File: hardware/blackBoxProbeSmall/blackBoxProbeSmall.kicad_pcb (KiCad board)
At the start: 4 copper layers, 44 x 29 mm, 79 parts, among them J1 USB-ID, J2 JTAG_2X05, J3 JTAG_2X05, J4 DevBoardUartInput, Q1 Q_NMOS_DUAL, Q2 Q_PMOS_DUAL, U1 MCP1702-MB, U2 USBLC6-2, U3 STM32F103CBT, U4 74X2T45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

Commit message: WIP routing/placement
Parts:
- removed R1, R13, R14, R15, R17, R19, R2, R21, R24, R25, R3, R4, R8, R9: 33, SquantorRcl:R_0402_hand
- removed R29, R30, R31, R32: 330, SquantorRcl:R_0402_hand
- removed R37, R38: 10K, SquantorRcl:R_0402_hand
- added RN1: 470, Resistor_SMD:R_Array_Convex_4x0402, F.Cu at (146.8, 106.8)
- added RN2: 47K, Resistor_SMD:R_Array_Convex_4x0402, F.Cu at (129.8, 98.8)
- added RN3: 33, Resistor_SMD:R_Array_Convex_4x0402, F.Cu at (129.8, 101.8)
- added RN4: 33, Resistor_SMD:R_Array_Convex_4x0402, F.Cu at (161.9, 96.7)
- J1: footprint SquantorUsb:SquantorUsb-USB-UB-SMD4H -> SquantorUsb:USB-muB-SMD_TH
- J4: value DevBoardUartInput -> DevBoardUartOutput
- N2: value V20190815 -> V20200131; footprint SquantorLabels:Label_version -> SquantorLabels:Label_Generic; moved to B.Cu
- moved R6 25.0 mm to (147.3, 87.6), turned to 270 degrees
- moved S1 24.5 mm to (152.2, 88.2)
- moved DA1 23.7 mm to (147.2, 110.7), turned to 0 degrees
- moved Q1 17.2 mm to (158.9, 88.9)
- moved R20 13.1 mm to (162.0, 94.7), turned to 0 degrees
- moved C14 12.5 mm to (153.1, 90.9), turned to 0 degrees
- moved F2 11.5 mm to (164.6, 101.7)
- moved R5 9.90 mm to (161.6, 105.4)
- moved Q2 5.38 mm to (156.0, 107.7)
- moved R28 5.38 mm to (153.7, 107.5)
- moved R10 0.74 mm to (161.6, 109.3), turned to 180 degrees
- moved C11 0.74 mm to (161.0, 111.0)
- moved R11 0.74 mm to (162.1, 111.0)
- moved N2 0.71 mm to (141.1, 95.7), turned to 180 degrees
- moved R33 0.20 mm to (161.6, 107.4)
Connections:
- J2 pad 2: /MCU_TMS -> Net-(J2-Pad2)
- J2 pad 4: /MCU_TCK -> Net-(J2-Pad4)
- J2 pad 6: /MCU_TDO -> Net-(J2-Pad6)
- J2 pad 7: Net-(J2-Pad7) -> (no net)
- J2 pad 8: /MCU_TDI -> Net-(J2-Pad8)
- J3 pad 4: /PROBE_E_TCK -> Net-(J3-Pad4)
- J3 pad 7: Net-(J3-Pad7) -> (no net)
- J3 pad 8: /PROBE_E_TDI -> Net-(J3-Pad8)
- J4 pad 4: /PROBE_E_TX -> Net-(J4-Pad4)
- R5 pad 1: /PROBE_E_TX -> Net-(J4-Pad4)
- R5 pad 2: Net-(R5-Pad2) -> /PROBE_E_TX
- U3 pad 10: Net-(U3-Pad10) -> (no net)
- U3 pad 11: Net-(R14-Pad1) -> /PROBE_TMS_DIR
- U3 pad 13: Net-(R15-Pad1) -> /PROBE_I_TDI
- U3 pad 14: Net-(R17-Pad1) -> /PROBE_I_TMS
- U3 pad 15: Net-(R19-Pad1) -> /PROBE_I_TCK
- U3 pad 2: Net-(U3-Pad2) -> (no net)
- U3 pad 27: Net-(U3-Pad27) -> (no net)
- U3 pad 28: Net-(U3-Pad28) -> (no net)
- U3 pad 3: Net-(U3-Pad3) -> (no net)
- U3 pad 30: Net-(R21-Pad1) -> /PROBE_I_TX
- U3 pad 39: Net-(R1-Pad1) -> /MCU_TDO
- U3 pad 4: Net-(U3-Pad4) -> (no net)
- U3 pad 43: Net-(U3-Pad43) -> (no net)
- U3 pad 45: Net-(U3-Pad45) -> (no net)
- U3 pad 46: Net-(U3-Pad46) -> (no net)
- U4 pad 6: Net-(R5-Pad2) -> /PROBE_E_TX
- U5 pad 6: Net-(R9-Pad2) -> /PROBE_E_TDI
- U5 pad 7: Net-(R8-Pad2) -> /PROBE_E_TCK
- U6 pad 2: Net-(R3-Pad1) -> /PROBE_I_TDO
- U6 pad 3: Net-(R4-Pad1) -> /PROBE_I_RX
- U7 pad 3: Net-(R2-Pad1) -> /PROBE_I_TMS
- U7 pad 6: Net-(R13-Pad2) -> /PROBE_E_TMS
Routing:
- net /PROBE_VDD: track 0.00 -> 24.2 mm
- net /BUTTON: track 17.3 -> 0.00 mm
- net /USB_PU: track 0.00 -> 14.4 mm
- net /USB_V: track 1.10 -> 14.0 mm
- net /MCU_RST: track 0.00 -> 12.1 mm, vias 0 -> 2
- net Net-(J2-Pad8): track 0.00 -> 4.92 mm
- net /MCU_TDI: track 8.99 -> 4.51 mm, vias 0 -> 1
- net Net-(J2-Pad6): track 0.00 -> 4.38 mm
- net Net-(J2-Pad4): track 0.00 -> 4.22 mm
- net Net-(J2-Pad2): track 0.00 -> 4.22 mm
- net Net-(R1-Pad1): track 3.76 -> 0.00 mm
- net /VSS: track 51.4 -> 48.3 mm, vias 14 -> 15
- net Net-(R21-Pad1): track 2.72 -> 0.00 mm
- net /PROBE_I_TDO: track 2.45 -> 0.00 mm
- net Net-(R15-Pad1): track 2.42 -> 0.00 mm
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
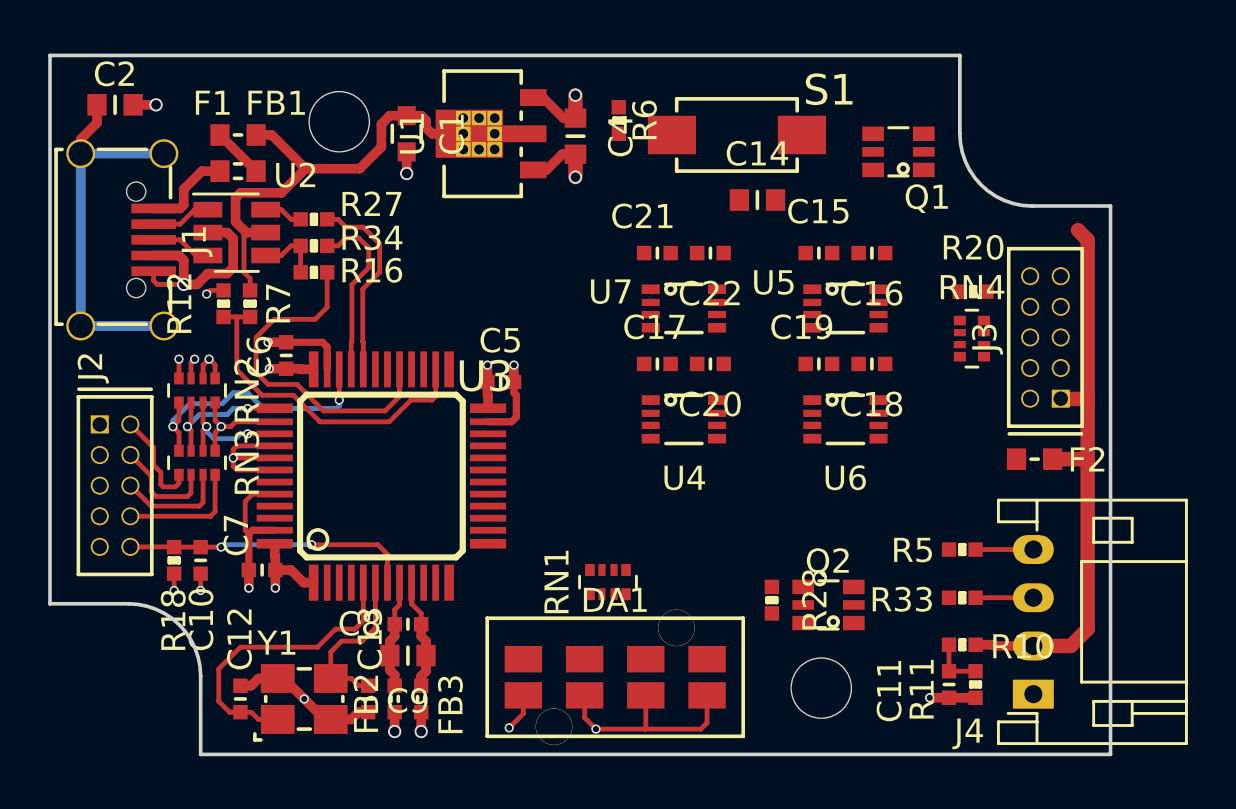
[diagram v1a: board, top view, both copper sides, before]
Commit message: WIP place/route, starting with level shifters
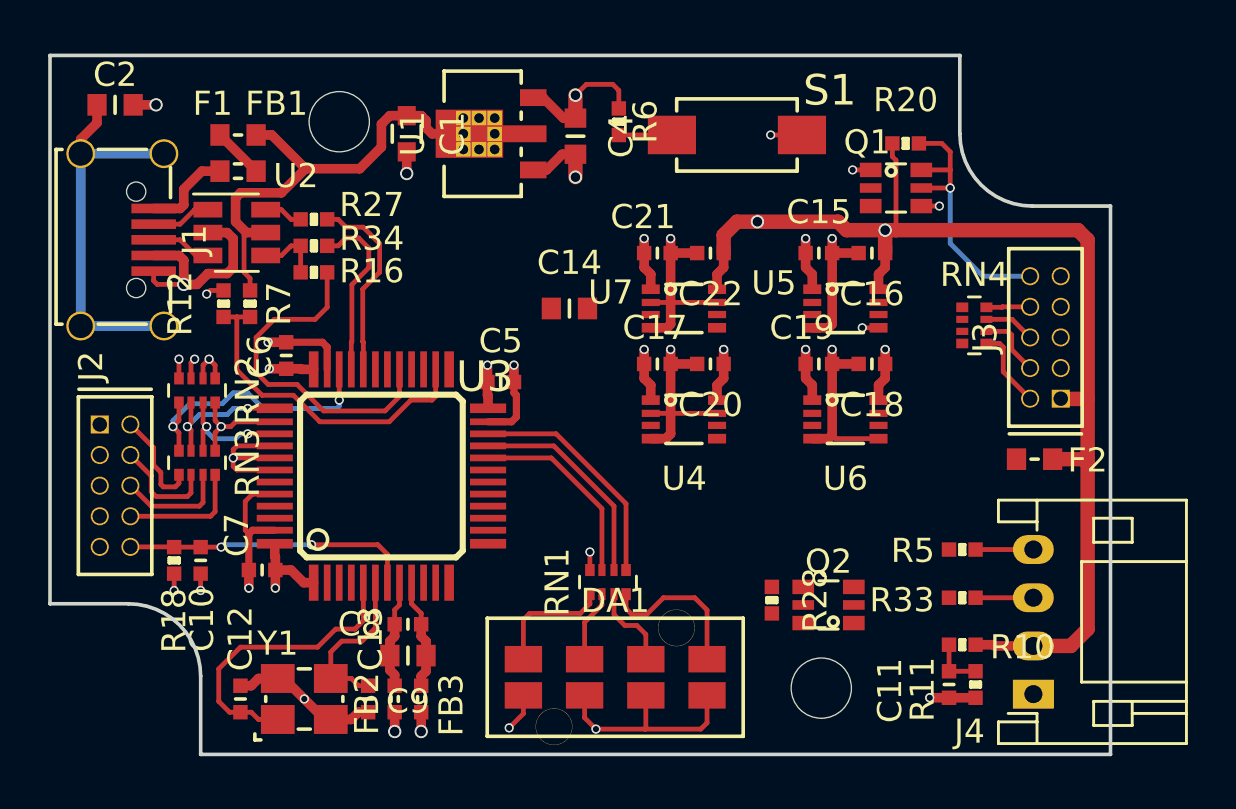
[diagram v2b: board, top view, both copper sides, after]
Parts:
- moved C14 9.00 mm to (145.2, 95.4)
- moved R20 6.76 mm to (159.2, 88.5)
- moved Q1 1.50 mm to (158.8, 90.4), turned to 270 degrees
- moved RN4 0.56 mm to (162.1, 96.1)
- moved R6 0.05 mm to (147.3, 87.7)
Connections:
- RN1 pad 1: Net-(DA1-Pad4) -> Net-(DA1-Pad1)
- RN1 pad 2: Net-(DA1-Pad3) -> Net-(DA1-Pad2)
- RN1 pad 3: Net-(DA1-Pad2) -> Net-(DA1-Pad3)
- RN1 pad 4: Net-(DA1-Pad1) -> Net-(DA1-Pad4)
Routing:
- net /PROBE_VDD: track 24.2 -> 64.0 mm, vias 0 -> 4
- net /VSS: track 48.3 -> 80.8 mm, vias 15 -> 22
- net /VDD: track 20.5 -> 33.5 mm, vias 9 -> 15
- net /PROBE_E_RST: track 0.00 -> 11.5 mm, vias 0 -> 1
- net /LED2: track 0.00 -> 9.68 mm
- net /LED1: track 0.00 -> 8.91 mm
- net /LED0: track 0.00 -> 8.14 mm
- net Net-(DA1-Pad4): track 0.00 -> 6.60 mm
- net Net-(DA1-Pad1): track 0.00 -> 5.07 mm
- net Net-(DA1-Pad3): track 0.00 -> 3.54 mm
- net Net-(J3-Pad2): track 0.00 -> 3.36 mm
- net Net-(DA1-Pad2): track 0.00 -> 3.00 mm
- net Net-(J3-Pad4): track 0.00 -> 2.80 mm
- net /BUTTON: track 0.00 -> 2.20 mm
- net Net-(J3-Pad6): track 0.00 -> 2.13 mm
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
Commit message: done place and route, silk placement starting
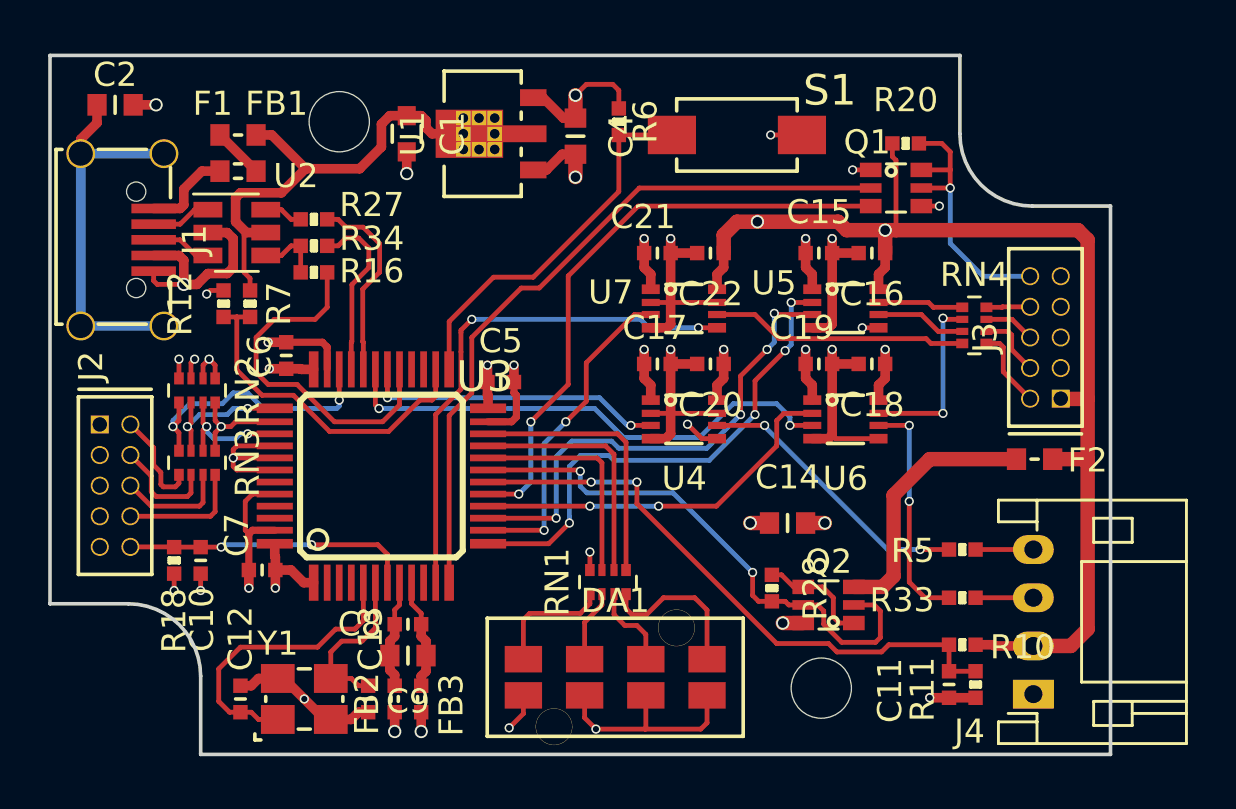
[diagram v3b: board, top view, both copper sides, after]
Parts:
- moved C14 12.7 mm to (154.3, 104.3)
- moved R28 0.50 mm to (153.7, 107.0)
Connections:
- U5 pad 2: /PROBE_I_TCK -> /PROBE_I_TDI
- U5 pad 3: /PROBE_I_TDI -> /PROBE_I_TCK
- U5 pad 6: /PROBE_E_TDI -> /PROBE_E_TCK
- U5 pad 7: /PROBE_E_TCK -> /PROBE_E_TDI
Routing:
- net /PROBE_I_RST: track 0.00 -> 29.7 mm
- net /PROBE_I_RST_SEN: track 0.00 -> 24.9 mm, vias 0 -> 2
- net /TARGET_PWR_EN: track 0.00 -> 22.9 mm, vias 0 -> 2
- net /TARGET_PWR_SENSE: track 2.20 -> 24.9 mm, vias 0 -> 2
- net /PROBE_TMS_DIR: track 0.00 -> 21.9 mm, vias 0 -> 2
- net /PROBE_I_RX: track 0.00 -> 21.3 mm, vias 0 -> 2
- net /PROBE_I_TDI: track 0.00 -> 21.0 mm, vias 0 -> 4
- net /PROBE_I_TCK: track 0.00 -> 20.4 mm, vias 0 -> 4
- net /PROBE_I_TDO: track 0.00 -> 15.7 mm, vias 0 -> 2
- net /BUTTON: track 2.20 -> 15.8 mm
- net /PROBE_I_TMS: track 0.00 -> 13.5 mm, vias 0 -> 2
- net /PROBE_I_TX: track 0.00 -> 12.6 mm, vias 0 -> 2
- net /PROBE_E_TX: track 0.00 -> 11.8 mm, vias 0 -> 2
- net Net-(F2-Pad2): track 0.00 -> 10.9 mm
- net /PROBE_E_TMS: track 0.00 -> 10.7 mm
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
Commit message: silk placement done, wait/review stage
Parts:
- moved N2 10.6 mm to (138.2, 105.9)
- moved N1 10.3 mm to (137.5, 102.1), turned to 180 degrees
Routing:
- net /PROBE_I_TX: track 12.6 -> 14.8 mm
- net /PROBE_I_RX: track 21.3 -> 22.1 mm
